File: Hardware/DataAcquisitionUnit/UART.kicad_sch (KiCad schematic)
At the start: 9 parts, among them J10 DE9_Pins_MountingHoles, J11 DE9_Pins_MountingHoles, J9 DE9_Pins_MountingHoles

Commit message: corections after hw sw integration
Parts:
- R21, R22, R23, R24, R25, R26: value 100R -> 22R
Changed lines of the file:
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@@
 			)
 		)
-		(property "Value" "100R"
+		(property "Value" "22R"
 			(at 96.52 125.3236 90)
 			(effects
@@
 		(fields_autoplaced yes)
 		(property "Reference" "R24"
-			(at 181.61 86.9856 90)
-			(effects
-				(font
-					(size 1.27 1.27)
-				)
-			)
-		)
-		(property "Value" "100R"
-			(at 181.61 89.7607 90)
+			(at 181.61 77.47 90)
+			(effects
+				(font
+					(size 1.27 1.27)
+				)
+			)
+		)
+		(property "Value" "22R"
+			(at 181.61 80.01 90)
 			(effects
 				(font
@@
 		(fields_autoplaced yes)
 		(property "Reference" "R26"
-			(at 96.52 136.5156 90)
-			(effects
-				(font
-					(size 1.27 1.27)
-				)
-			)
-		)
-		(property "Value" "100R"
-			(at 96.52 139.2907 90)
+			(at 96.52 137.16 90)
+			(effects
+				(font
+					(size 1.27 1.27)
+				)
+			)
+		)
+		(property "Value" "22R"
+			(at 96.52 139.7 90)
 			(effects
 				(font
@@
 			)
 		)
-		(property "Value" "100R"
+		(property "Value" "22R"
 			(at 181.61 75.7936 90)
 			(effects
@@
 			)
 		)
-		(property "Value" "100R"
+		(property "Value" "22R"
 			(at 97.79 75.7936 90)
 			(effects
@@
 		(fields_autoplaced yes)
 		(property "Reference" "R22"
-			(at 97.79 86.9856 90)
-			(effects
-				(font
-					(size 1.27 1.27)
-				)
-			)
-		)
-		(property "Value" "100R"
-			(at 97.79 89.7607 90)
-			(effects
-				(font
+			(at 97.79 87.63 90)
+			(effects
+				(font
+					(size 1.27 1.27)
+				)
+			)
+		)
+		(property "Value" "22R"
+			(at 97.79 90.17 90)
+			(effects
+				(font

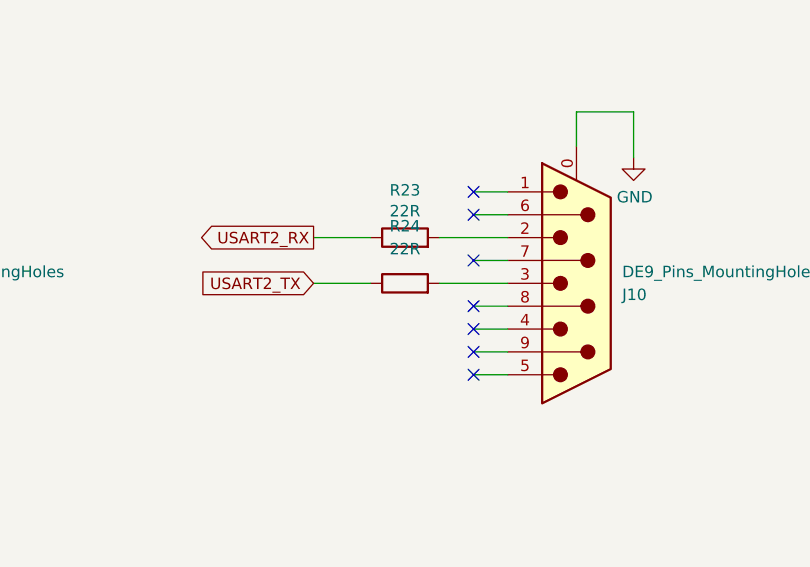
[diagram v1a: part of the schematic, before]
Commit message: rework CI, make PCB smaller
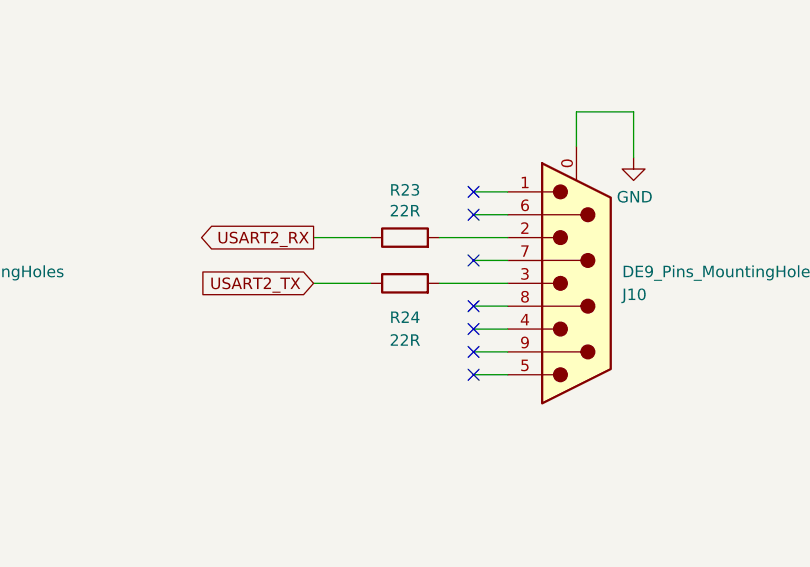
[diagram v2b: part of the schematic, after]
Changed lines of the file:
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@@
 		(fields_autoplaced yes)
 		(property "Reference" "R24"
-			(at 181.61 77.47 90)
+			(at 181.61 87.63 90)
 			(effects
 				(font
@@
 		)
 		(property "Value" "22R"
-			(at 181.61 80.01 90)
+			(at 181.61 90.17 90)
 			(effects
 				(font
